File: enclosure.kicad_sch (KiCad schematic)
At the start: 0 parts

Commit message: import schematic settings from pss
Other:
- company: (none) -> Open Battery Tester
- title: (none) -> Enclosure
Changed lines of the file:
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@@
 	(generator_version "8.0")
 	(paper "A4")
+	(title_block
+		(title "Enclosure")
+		(date "2025-02-20")
+		(rev "0.0.0")
+		(company "Open Battery Tester")
+		(comment 1 "Overview")
+	)
 	(sheet_instances
 		(path "/"

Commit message: add digital-interface from pss
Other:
- added sheet digital-interface (digital-interface.kicad_sch)
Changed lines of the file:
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@@
 		(comment 1 "Overview")
+	)
+	(sheet
+		(at 25.4 25.4)
+		(size 25.4 15.24)
+		(fields_autoplaced yes)
+		(stroke
+			(width 0.1524)
+			(type solid)
+		)
+		(fill
+			(color 0 0 0 0.0000)
+		)
+		(property "Sheetname" "digital-interface"
+			(at 25.4 24.6884 0)
+			(effects
+				(font
+					(size 1.27 1.27)
+				)
+				(justify left bottom)
+			)
+		)
+		(property "Sheetfile" "digital-interface.kicad_sch"
+			(at 25.4 41.2246 0)
+			(effects
+				(font
+					(size 1.27 1.27)
+				)
+				(justify left top)
+			)
+		)
+		(instances
+			(project "enclosure"
+				(path "/8ec0899b-9d7b-491d-933a-49b74b34a0df"
+					(page "2")
+				)
+			)
+		)
 	)
 	(sheet_instances

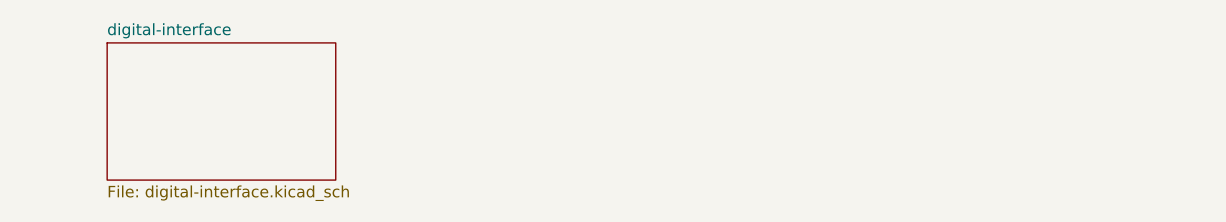
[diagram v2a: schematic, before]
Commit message: add enclosure integration of digital-interface in overview
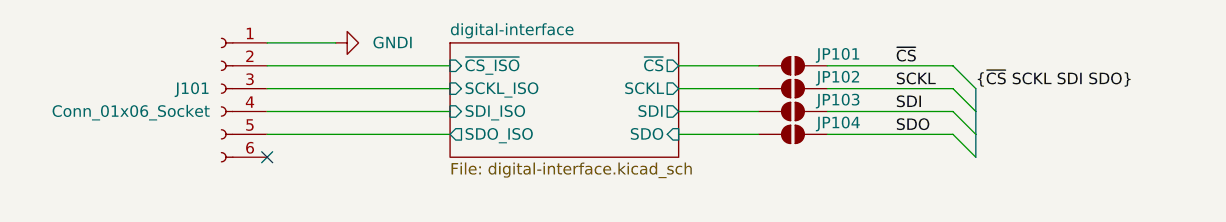
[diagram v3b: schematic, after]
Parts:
- added J101: Conn_01x06_Socket, pss:PhoenixContact_TDPT_2,5_6-SP-5,08_1x06_P5.08mm_Horizontal, symbol pss:Conn_01x06_Socket
- added JP101, JP102, JP103, JP104: SolderJumper_2_Open, pss:SolderJumper-2_P1.3mm_Open_RoundedPad1.0x1.5mm, symbol pss:SolderJumper_2_Open
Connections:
- new net GNDI: J101.1 (Pin_1)
- new net SCKL: JP102.2 (B)
- new net SDI: JP103.2 (B)
- new net SDO: JP104.2 (B)
- new net digital-interface/SCKL: JP102.1 (A)
- new net digital-interface/SCKL_ISO: J101.3 (Pin_3)
- new net digital-interface/SDI: JP103.1 (A)
- new net digital-interface/SDI_ISO: J101.4 (Pin_4)
- new net digital-interface/SDO: JP104.1 (A)
- new net digital-interface/SDO_ISO: J101.5 (Pin_5)
- new net digital-interface/~{CS_ISO}: J101.2 (Pin_2)
- new net digital-interface/~{CS}: JP101.1 (A)
- new net ~{CS}: JP101.2 (B)
- no-connect marks 0 -> 1
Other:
- sheet digital-interface ports: added SCKL, SCKL_ISO, SDI, SDI_ISO, SDO, SDO_ISO, ~{CS_ISO}, ~{CS}; removed none

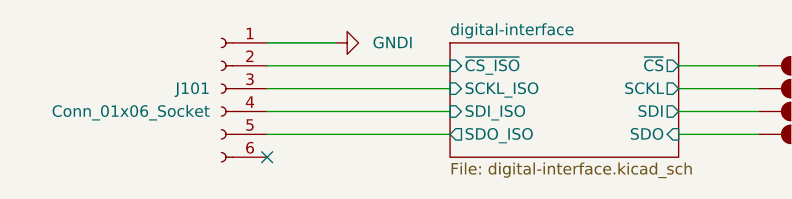
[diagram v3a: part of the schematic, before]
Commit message: fix enclosure digital-interface stray wire in schmematic
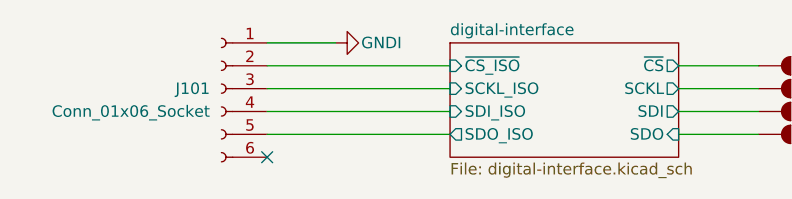
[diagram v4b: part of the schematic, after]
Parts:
- removed JP102, JP103, JP104: SolderJumper_2_Open, pss:SolderJumper-2_P1.3mm_Open_RoundedPad1.0x1.5mm, symbol pss:SolderJumper_2_Open
- added JP102, JP103, JP104: SolderJumper_2_Open, pss:SolderJumper-2_P1.3mm_Open_RoundedPad1.0x1.5mm, symbol enclosure:SolderJumper_2_Open
- J101: symbol pss:Conn_01x06_Socket -> enclosure:Conn_01x06_Socket
- JP101: symbol pss:SolderJumper_2_Open -> enclosure:SolderJumper_2_Open
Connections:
- net SCKL: now also JP102.2 (B)
- net SDI: now also JP103.2 (B)
- net SDO: now also JP104.2 (B)
- net digital-interface/SCKL: now also JP102.1 (A)
- net digital-interface/SDI: now also JP103.1 (A)
- net digital-interface/SDO: now also JP104.1 (A)
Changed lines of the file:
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@@
 	)
 	(symbol
-		(lib_id "pss:Conn_01x06_Socket")
+		(lib_id "enclosure:SolderJumper_2_Open")
+		(at 101.6 30.48 0)
+		(unit 1)
+		(exclude_from_sim yes)
+		(in_bom no)
+		(on_board yes)
+		(dnp no)
+		(property "Reference" "JP102"
+			(at 106.68 29.21 0)
+			(effects
+				(font
+					(size 1.27 1.27)
+				)
+			)
+		)
+		(property "Value" "SolderJumper_2_Open"
+			(at 76.2 17.78 0)
+			(effects
+				(font
+					(size 1.27 1.27)
+				)
+				(hide yes)
+			)
+		)
+		(property "Footprint" "pss:SolderJumper-2_P1.3mm_Open_RoundedPad1.0x1.5mm"
+			(at 101.6 30.48 0)
+			(effects
+				(font
+					(size 1.27 1.27)
+				)
+				(hide yes)
+			)
+		)
+		(property "Datasheet" "~"
+			(at 101.6 30.48 0)
+			(effects
+				(font
+					(size 1.27 1.27)
+				)
+				(hide yes)
+			)
+		)
+		(property "Description" "Solder Jumper, 2-pole, open"
+			(at 101.6 30.48 0)
+			(effects
+				(font
+					(size 1.27 1.27)
+				)
+				(hide yes)
+			)
+		)
+		(pin "1"
+		)
+		(pin "2"
+		)
+		(instances
+			(project "enclosure"
+				(path "/8ec0899b-9d7b-491d-933a-49b74b34a0df"
+					(reference "JP102")
+					(unit 1)
+				)
+			)
+		)
+	)
+	(symbol
+		(lib_id "enclosure:Conn_01x06_Socket")
 		(at 38.1 30.48 0)
 		(mirror y)
@@
 	)
 	(symbol
-		(lib_id "pss:GNDI")
+		(lib_id "enclosure:SolderJumper_2_Open")
+		(at 101.6 35.56 0)
+		(unit 1)
+		(exclude_from_sim yes)
+		(in_bom no)
+		(on_board yes)
+		(dnp no)
+		(property "Reference" "JP104"
+			(at 106.68 34.29 0)
+			(effects
+				(font
+					(size 1.27 1.27)
+				)
+			)
+		)
+		(property "Value" "SolderJumper_2_Open"
+			(at 76.2 22.86 0)
+			(effects
+				(font
+					(size 1.27 1.27)
+				)
+				(hide yes)
+			)
+		)
+		(property "Footprint" "pss:SolderJumper-2_P1.3mm_Open_RoundedPad1.0x1.5mm"
+			(at 101.6 35.56 0)
+			(effects
+				(font
+					(size 1.27 1.27)
+				)
+				(hide yes)
+			)
+		)
+		(property "Datasheet" "~"
+			(at 101.6 35.56 0)
+			(effects
+				(font
+					(size 1.27 1.27)
+				)
+				(hide yes)
+			)
+		)
+		(property "Description" "Solder Jumper, 2-pole, open"
+			(at 101.6 35.56 0)
+			(effects
+				(font
+					(size 1.27 1.27)
+				)
+				(hide yes)
+			)
+		)
+		(pin "1"
+		)
+		(pin "2"
+		)
+		(instances
+			(project "enclosure"
+				(path "/8ec0899b-9d7b-491d-933a-49b74b34a0df"
+					(reference "JP104")
+					(unit 1)
+				)
+			)
+		)
+	)
+	(symbol
+		(lib_id "enclosure:SolderJumper_2_Open")
+		(at 101.6 27.94 0)
+		(unit 1)
+		(exclude_from_sim yes)
+		(in_bom no)
+		(on_board yes)
+		(dnp no)
+		(property "Reference" "JP101"
+			(at 106.68 26.67 0)
+			(effects
+				(font
+					(size 1.27 1.27)
+				)
+			)
+		)
+		(property "Value" "SolderJumper_2_Open"
+			(at 76.2 15.24 0)
+			(effects
+				(font
+					(size 1.27 1.27)
+				)
+				(hide yes)
+			)
+		)
+		(property "Footprint" "pss:SolderJumper-2_P1.3mm_Open_RoundedPad1.0x1.5mm"
+			(at 101.6 27.94 0)
+			(effects
+				(font
+					(size 1.27 1.27)
+				)
+				(hide yes)
+			)
+		)
+		(property "Datasheet" "~"
+			(at 101.6 27.94 0)
+			(effects
+				(font
+					(size 1.27 1.27)
+				)
+				(hide yes)
+			)
+		)
+		(property "Description" "Solder Jumper, 2-pole, open"
+			(at 101.6 27.94 0)
+			(effects
+				(font
+					(size 1.27 1.27)
+				)
+				(hide yes)
+			)
+		)
+		(pin "1"
+		)
+		(pin "2"
+		)
+		(instances
+			(project "enclosure"
+				(path "/8ec0899b-9d7b-491d-933a-49b74b34a0df"
+					(reference "JP101")
+					(unit 1)
+				)
+			)
+		)
+	)
+	(symbol
+		(lib_id "enclosure:GNDI")
 		(at 50.8 25.4 90)
 		(unit 1)
@@
 		)
 		(property "Value" "GNDI"
-			(at 57.15 25.4 90)
+			(at 55.88 25.4 90)
 			(effects
 				(font
@@
 	)
 	(symbol
-		(lib_id "pss:SolderJumper_2_Open")
-		(at 101.6 27.94 0)
+		(lib_id "enclosure:SolderJumper_2_Open")
+		(at 101.6 33.02 0)
 		(unit 1)
 		(exclude_from_sim yes)
@@
 		(on_board yes)
 		(dnp no)
-		(property "Reference" "JP101"
-			(at 106.68 26.67 0)
-			(effects
-				(font
-					(size 1.27 1.27)
-				)
-			)
-		)
-		(property "Value" "SolderJumper_2_Open"
-			(at 76.2 15.24 0)
-			(effects
-				(font
-					(size 1.27 1.27)
-				)
-				(hide yes)
-			)
-		)
-		(property "Footprint" "pss:SolderJumper-2_P1.3mm_Open_RoundedPad1.0x1.5mm"
-			(at 101.6 27.94 0)
-			(effects
-				(font
-					(size 1.27 1.27)
-				)
-				(hide yes)
-			)
-		)
-		(property "Datasheet" "~"
-			(at 101.6 27.94 0)
-			(effects
-				(font
-					(size 1.27 1.27)
-				)
-				(hide yes)
-			)
-		)
-		(property "Description" "Solder Jumper, 2-pole, open"
-			(at 101.6 27.94 0)
-			(effects
-				(font
-					(size 1.27 1.27)
-				)
-				(hide yes)
-			)
-		)
-		(pin "1"
-		)
-		(pin "2"
-		)
-		(instances
-			(project "enclosure"
-				(path "/8ec0899b-9d7b-491d-933a-49b74b34a0df"
-					(reference "JP101")
-					(unit 1)
-				)
-			)
-		)
-	)
-	(symbol
-		(lib_id "pss:SolderJumper_2_Open")
-		(at 101.6 33.02 0)
-		(unit 1)
-		(exclude_from_sim yes)
-		(in_bom no)
-		(on_board yes)
-		(dnp no)
 		(property "Reference" "JP103"
 			(at 106.68 31.75 0)
@@
 					(unit 1)
 				)
-			)
-		)
-	)
-	(symbol
-		(lib_id "pss:SolderJumper_2_Open")
-		(at 101.6 35.56 0)
-		(unit 1)
-		(exclude_from_sim yes)
-		(in_bom no)
-		(on_board yes)
-		(dnp no)
-		(property "Reference" "JP104"
-			(at 106.68 34.29 0)
-			(effects
-				(font
-					(size 1.27 1.27)
-				)
-			)
-		)
-		(property "Value" "SolderJumper_2_Open"
-			(at 76.2 22.86 0)
-			(effects
-				(font
-					(size 1.27 1.27)
-				)
-				(hide yes)
-			)
-		)
-		(property "Footprint" "pss:SolderJumper-2_P1.3mm_Open_RoundedPad1.0x1.5mm"
-			(at 101.6 35.56 0)
-			(effects
-				(font
-					(size 1.27 1.27)
-				)
-				(hide yes)
-			)
-		)
-		(property "Datasheet" "~"
-			(at 101.6 35.56 0)
-			(effects
-				(font
-					(size 1.27 1.27)
-				)
-				(hide yes)
-			)
-		)
-		(property "Description" "Solder Jumper, 2-pole, open"
-			(at 101.6 35.56 0)
-			(effects
-				(font
-					(size 1.27 1.27)
-				)
-				(hide yes)
-			)
-		)
-		(pin "1"
-		)
-		(pin "2"
-		)
-		(instances
-			(project "enclosure"
-				(path "/8ec0899b-9d7b-491d-933a-49b74b34a0df"
-					(reference "JP104")
-					(unit 1)
-				)
-			)
-		)
-	)
-	(symbol
-		(lib_id "pss:SolderJumper_2_Open")
-		(at 101.6 30.48 0)
-		(unit 1)
-		(exclude_from_sim yes)
-		(in_bom no)
-		(on_board yes)
-		(dnp no)
-		(property "Reference" "JP102"
-			(at 106.68 29.21 0)
-			(effects
-				(font
-					(size 1.27 1.27)
-				)
-			)
-		)
-		(property "Value" "SolderJumper_2_Open"
-			(at 76.2 17.78 0)
-			(effects
-				(font
-					(size 1.27 1.27)
-				)
-				(hide yes)
-			)
-		)
-		(property "Footprint" "pss:SolderJumper-2_P1.3mm_Open_RoundedPad1.0x1.5mm"
-			(at 101.6 30.48 0)
-			(effects
-				(font
-					(size 1.27 1.27)
-				)
-				(hide yes)
-			)
-		)
-		(property "Datasheet" "~"
-			(at 101.6 30.48 0)
-			(effects
-				(font
-					(size 1.27 1.27)
-				)
-				(hide yes)
-			)
-		)
-		(property "Description" "Solder Jumper, 2-pole, open"
-			(at 101.6 30.48 0)
-			(effects
-				(font
-					(size 1.27 1.27)
-				)
-				(hide yes)
-			)
-		)
-		(pin "1"
-		)
-		(pin "2"
-		)
-		(instances
-			(project "enclosure"
-				(path "/8ec0899b-9d7b-491d-933a-49b74b34a0df"
-					(reference "JP102")
-					(unit 1)
-				)

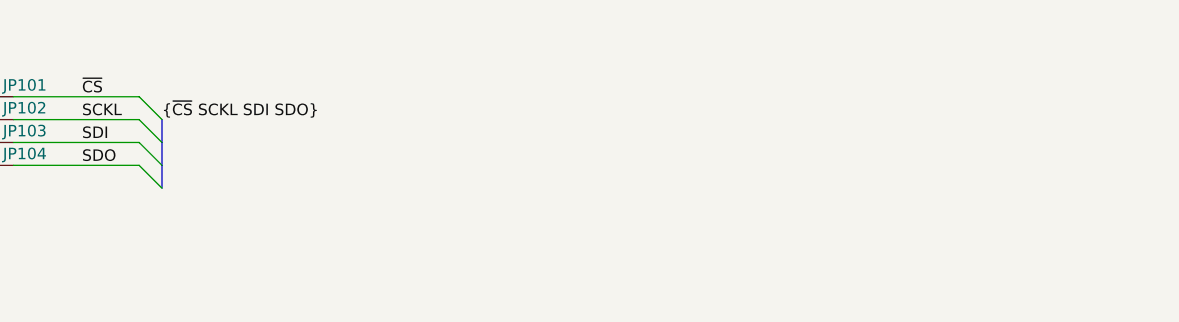
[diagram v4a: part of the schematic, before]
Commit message: add enclosure dac sub circuit
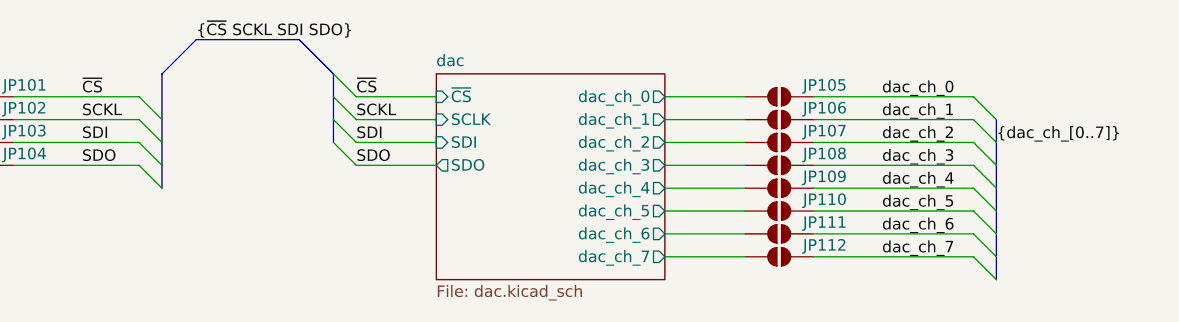
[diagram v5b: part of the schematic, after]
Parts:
- added JP105, JP106, JP107, JP108, JP109, JP110, JP111, JP112: SolderJumper_2_Open, pss:SolderJumper-2_P1.3mm_Open_RoundedPad1.0x1.5mm, symbol enclosure:SolderJumper_2_Open
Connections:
- new net dac/dac_ch_0: JP105.1 (A)
- new net dac/dac_ch_1: JP106.1 (A)
- new net dac/dac_ch_2: JP107.1 (A)
- new net dac/dac_ch_3: JP108.1 (A)
- new net dac/dac_ch_4: JP109.1 (A)
- new net dac/dac_ch_5: JP110.1 (A)
- new net dac/dac_ch_6: JP111.1 (A)
- new net dac/dac_ch_7: JP112.1 (A)
- new net dac_ch_0: JP105.2 (B)
- new net dac_ch_1: JP106.2 (B)
- new net dac_ch_2: JP107.2 (B)
- new net dac_ch_3: JP108.2 (B)
- new net dac_ch_4: JP109.2 (B)
- new net dac_ch_5: JP110.2 (B)
- new net dac_ch_6: JP111.2 (B)
- new net dac_ch_7: JP112.2 (B)
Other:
- added sheet dac (dac.kicad_sch)
- title: Enclosure -> Power Supply Sink

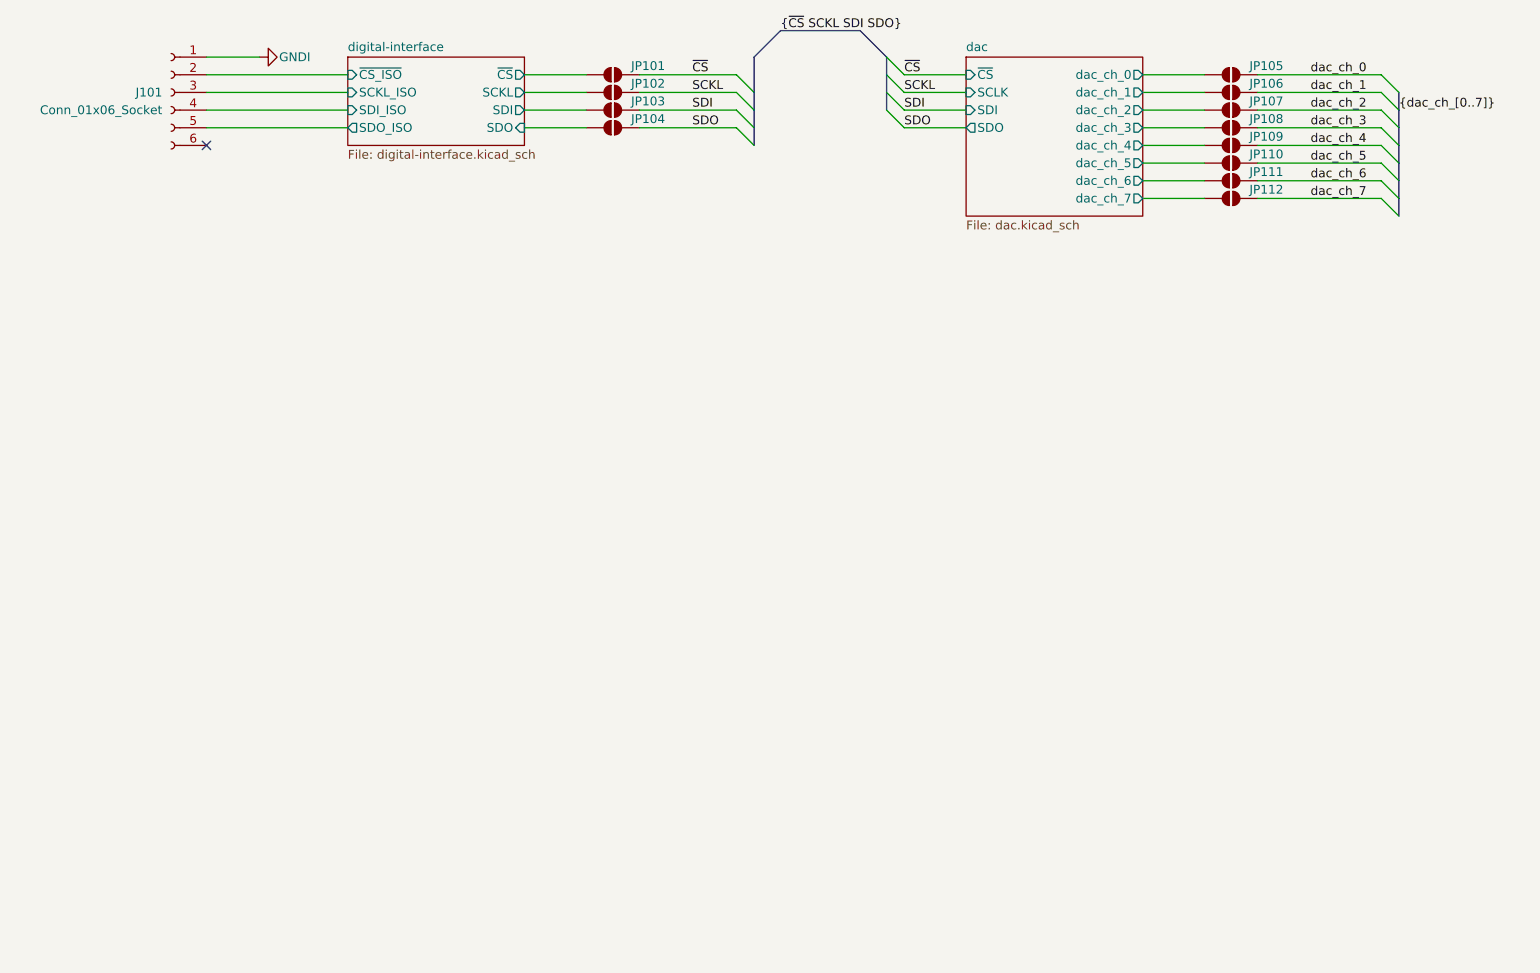
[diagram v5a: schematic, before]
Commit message: add enclosure pwm sub circuit
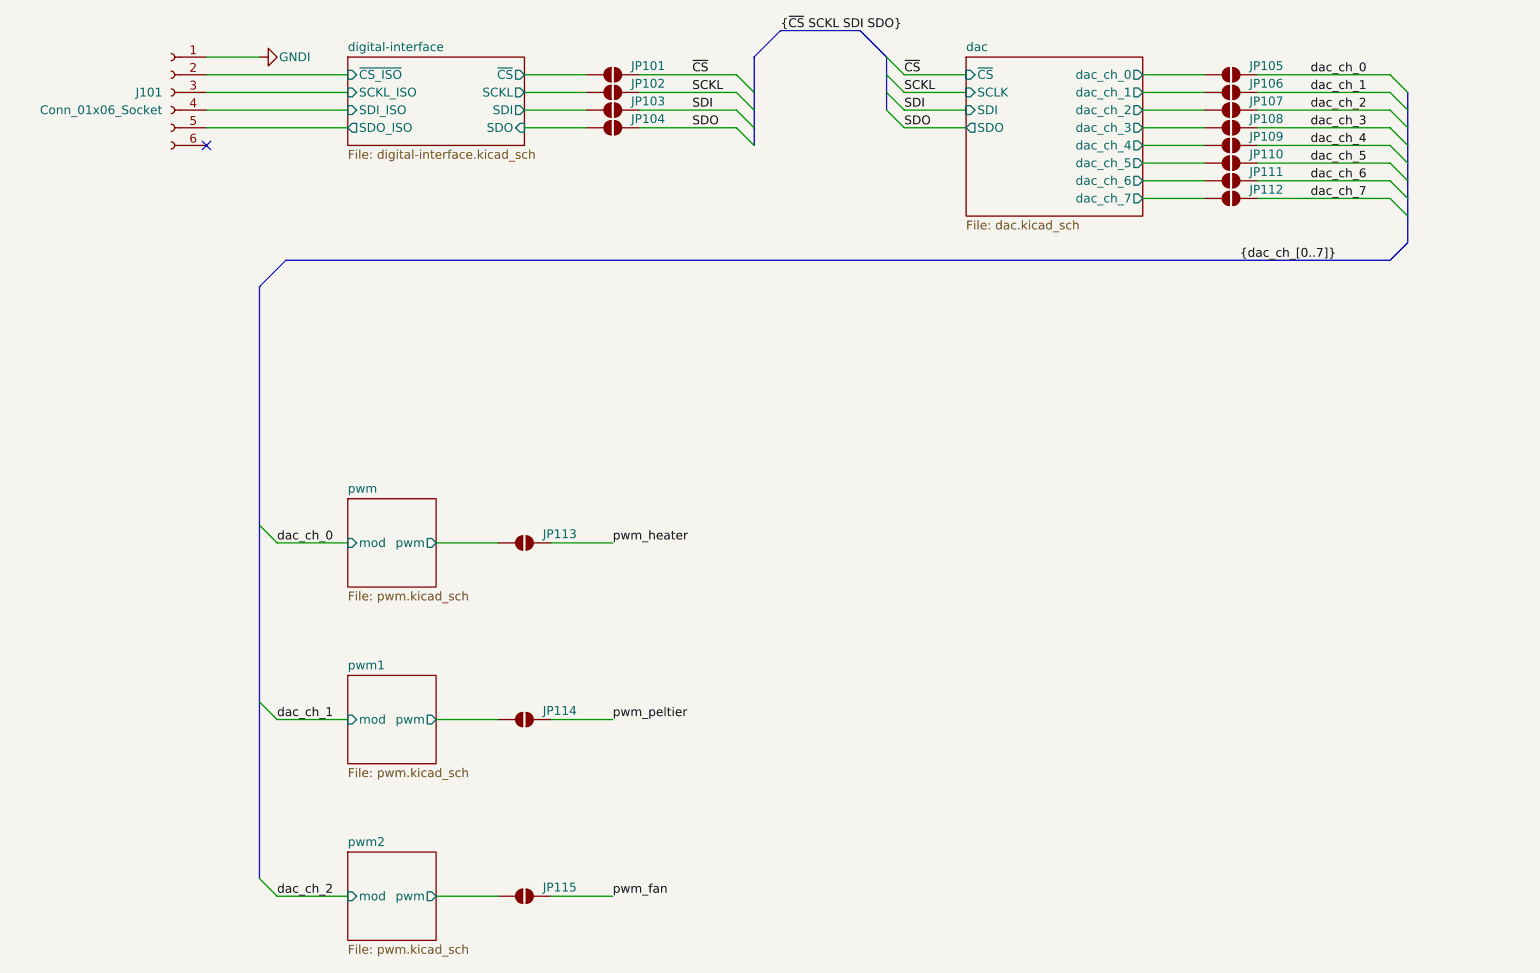
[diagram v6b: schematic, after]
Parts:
- added JP113, JP114, JP115: SolderJumper_2_Open, pss:SolderJumper-2_P1.3mm_Open_RoundedPad1.0x1.5mm, symbol enclosure:SolderJumper_2_Open
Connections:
- new net pwm/pwm: JP113.1 (A)
- new net pwm1/pwm: JP114.1 (A)
- new net pwm2/pwm: JP115.1 (A)
- new net pwm_fan: JP115.2 (B)
- new net pwm_heater: JP113.2 (B)
- new net pwm_peltier: JP114.2 (B)
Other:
- added sheet pwm (pwm.kicad_sch)
- added sheet pwm1 (pwm.kicad_sch)
- added sheet pwm2 (pwm.kicad_sch)
